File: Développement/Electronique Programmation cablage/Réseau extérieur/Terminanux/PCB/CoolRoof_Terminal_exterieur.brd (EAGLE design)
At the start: 48 x 38.5 mm, 7 parts, among them U100 XBEE, U201 COMMUTATEUR_GLISSIERE_1RT_100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, U202 MCP1700T-3302E/TT

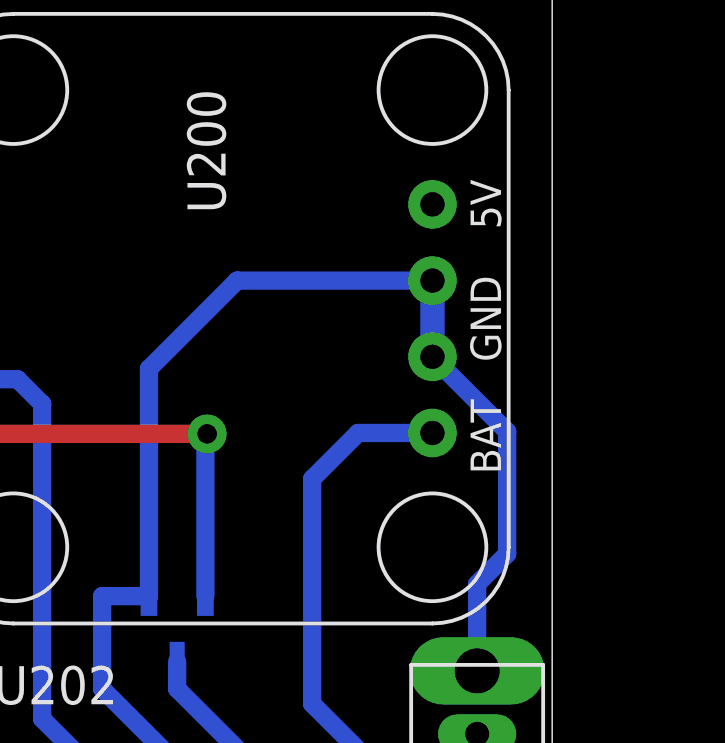
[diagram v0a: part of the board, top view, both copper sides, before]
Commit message: Remplacement du microchargeur par version aux pastilles plus larges
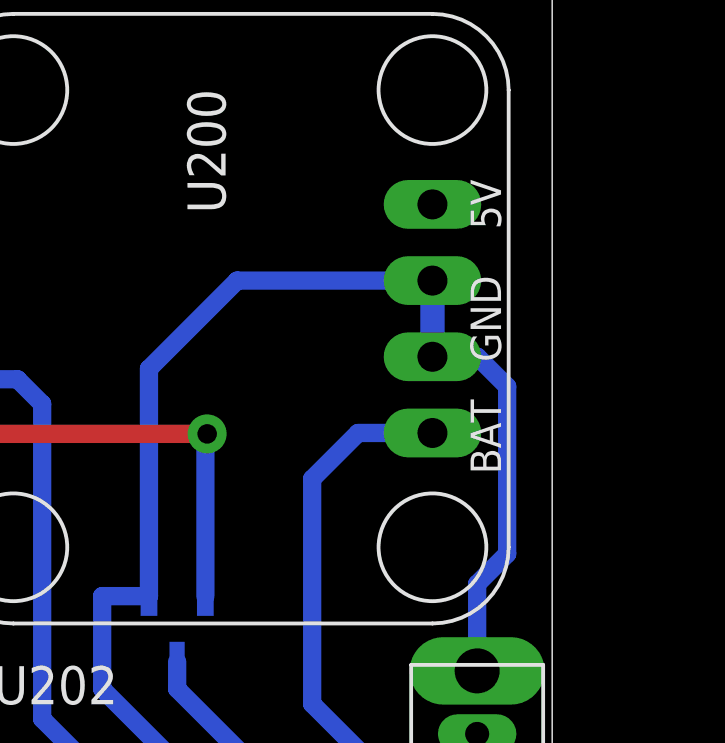
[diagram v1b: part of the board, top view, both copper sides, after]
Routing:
- net GND: track 117.5 -> 118.4 mm
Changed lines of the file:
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@@
 <?xml version="1.0" encoding="utf-8"?>
 <!DOCTYPE eagle SYSTEM "eagle.dtd">
-<eagle version="8.4.0">
+<eagle version="9.5.2">
 <drawing>
 <settings>
@@
 <param name="dpMaxLengthDifference" value="10mm"/>
 <param name="dpGapFactor" value="2.5"/>
+<param name="checkAngle" value="0"/>
 <param name="checkFont" value="1"/>
 <param name="checkRestrict" value="1"/>
 <param name="checkStop" value="0"/>
+<param name="checkValues" value="0"/>
+<param name="checkNames" value="1"/>
+<param name="checkWireStubs" value="1"/>
+<param name="checkPolygonWidth" value="0"/>
 <param name="useDiameter" value="13"/>
 <param name="maxErrors" value="50"/>
@@
 <wire x1="58" y1="16.1" x2="58" y2="19" width="0.6096" layer="16"/>
 <wire x1="58" y1="19" x2="59" y2="20" width="0.6096" layer="16"/>
-<wire x1="59" y1="20" x2="59" y2="24.08" width="0.6096" layer="16"/>
-<wire x1="59" y1="24.08" x2="56.51" y2="26.57" width="0.6096" layer="16"/>
+<wire x1="59" y1="20" x2="59" y2="25.58" width="0.6096" layer="16"/>
+<wire x1="59" y1="25.58" x2="58.01" y2="26.57" width="0.6096" layer="16"/>
+<wire x1="58.01" y1="26.57" x2="56.51" y2="26.57" width="0.6096" layer="16"/>
 </signal>
 <signal name="N$7">
@@
 </signal>
 </signals>
+<mfgpreviewcolors>
+<mfgpreviewcolor name="soldermaskcolor" color="0xC8008000"/>
+<mfgpreviewcolor name="silkscreencolor" color="0xFFFEFEFE"/>
+<mfgpreviewcolor name="backgroundcolor" color="0xFF282828"/>
+<mfgpreviewcolor name="coppercolor" color="0xFFFFBF00"/>
+<mfgpreviewcolor name="substratecolor" color="0xFF786E46"/>
+</mfgpreviewcolors>
 </board>
 </drawing>
